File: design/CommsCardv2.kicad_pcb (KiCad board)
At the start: 4 copper layers, 191 parts, among them J1001 USB_B, J201 Conn_01x02, J301 DB9_Male_MountingHoles, J302 DB9_Male_MountingHoles, J303 DB9_Male_MountingHoles, J304 Conn_01x02, J305 Conn_Coaxial, J501 Conn_01x03, J701 Conn_01x03, J901 USB_B, Q301 Q_NMOS_DGS, Q302 Q_NMOS_DGS, U1001 ADUM3160, U201 LT3509EMSE, U301 MAX3387EEUG, U302 MAX3485, U303 TPS28225DRBT, U401 74LV14, U402 74LVC2G00, U403 STWD100xxWY, U404 STWD100xxWY, U405 74AHC157, U501 93C46B, U502 FT4232H, U503 74LV595, U601 74LVC3G14, U602 SN74LV86, U603 501BMILF, U604 74LVC1G80, U605 74LV595, U606 74LV595, U701 93C46B, U702 FT4232H, U703 74LV595, U801 74LVC3G14, U802 SN74LV86, U803 501BMILF, U804 74LVC1G80, U805 74LV595, U806 74LV595, U901 ADUM3160, X501 ASEMB-12MHz, X701 ASEMB-12MHz

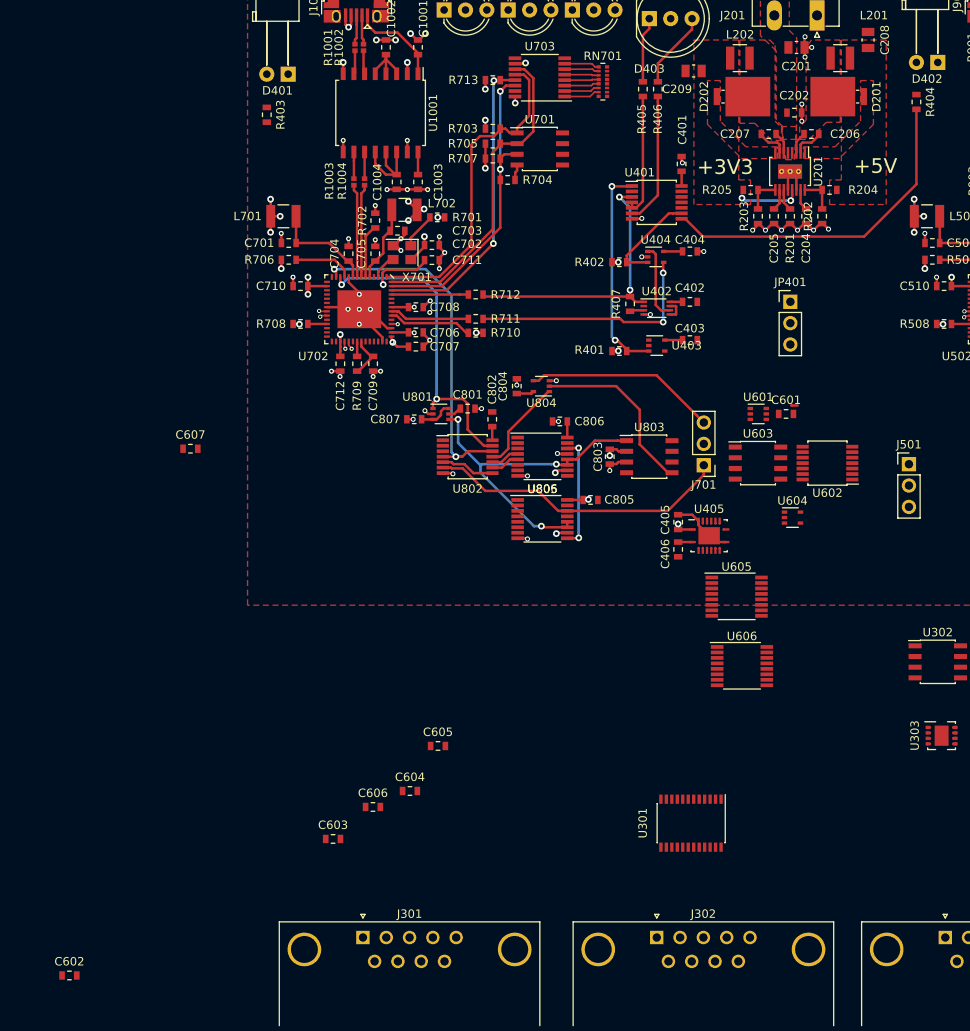
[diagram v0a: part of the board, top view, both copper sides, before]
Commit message: Further LOS updates.  Compressing space
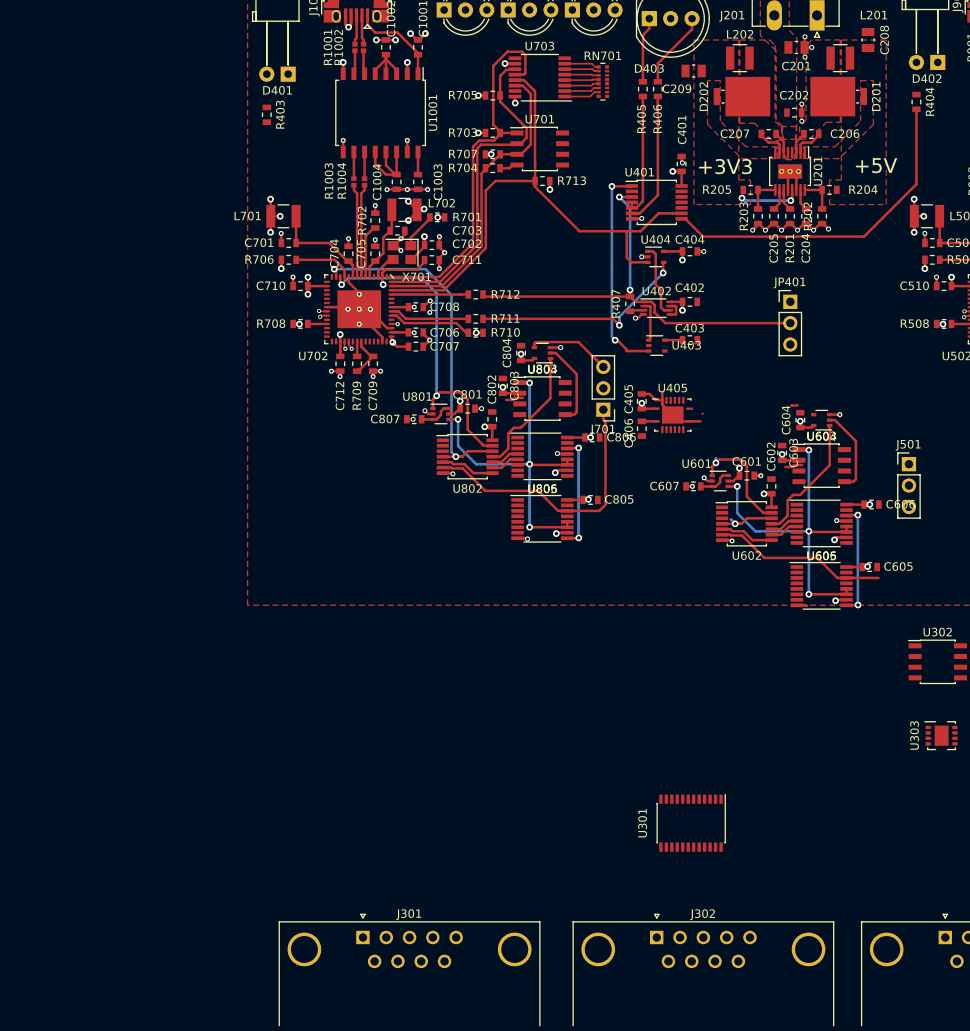
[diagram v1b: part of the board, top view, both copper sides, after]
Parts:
- removed R401, R402: 10k, Resistor_SMD:R_0603_1608Metric
- moved C602 101.7 mm to (137.5, 98.8), turned to 90 degrees
- moved C603 70.4 mm to (138.7, 94.8), turned to 90 degrees
- moved C606 69.3 mm to (149.4, 100.9)
- moved C604 64.0 mm to (140.9, 90.9), turned to 90 degrees
- moved C607 60.0 mm to (128.2, 98.8), turned to 180 degrees
- moved C605 55.6 mm to (149.1, 108.4)
- moved U606 19.4 mm to (143.4, 103.2)
- moved C803 15.2 mm to (105.5, 86.8), turned to 90 degrees
- moved C405 15.0 mm to (122.0, 88.7)
- moved C406 15.0 mm to (122.0, 91.9)
- moved U405 15.0 mm to (125.7, 90.3)
- moved U803 14.5 mm to (110.2, 88.3)
- moved J701 13.6 mm to (117.5, 89.7)
- moved R713 13.4 mm to (110.2, 62.5), turned to 0 degrees
- moved U604 12.1 mm to (143.4, 90.9), turned to 180 degrees
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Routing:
- net /FlightComputer1/LOSComms/DELAY_CLK: track 0.00 -> 42.3 mm, vias 0 -> 4
- net (no net): track 0.00 -> 23.1 mm, vias 0 -> 1
- net +3V3: track 107.9 -> 129.0 mm, vias 46 -> 60
- net /FlightComputer1/LOSComms/RNRZ-L: track 0.00 -> 20.7 mm
- net /Watchdog/~FC2_PWREN: track 48.2 -> 67.5 mm, vias 2 -> 0
- net /FlightComputer1/IN_CHARGE: track 35.0 -> 54.0 mm
- net /FlightComputer1/LOSComms/CLK: track 0.00 -> 13.8 mm, vias 0 -> 1
- net Net-(U605-Pad9): track 0.00 -> 13.5 mm, vias 0 -> 2
- net /FlightComputer2/LOSComms/BIPHASE: track 22.9 -> 9.97 mm
- net /FlightComputer2/LOSComms/2xCLOCK: track 21.3 -> 10.2 mm
- net /FlightComputer1/LOSComms/2xCLOCK: track 0.00 -> 10.2 mm
- net GND: track 119.5 -> 128.0 mm, vias 80 -> 82
- net /FlightComputer2/EECS: track 38.9 -> 45.8 mm
- net Net-(U602-Pad5): track 0.00 -> 6.44 mm
- net /Watchdog/FC1_WDO: track 0.00 -> 4.86 mm
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
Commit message: Minimizing space in design
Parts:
- D403: footprint LED_THT:LED_D8.0mm-3 -> LEDs:WP130WDT
- D501, D502, D503, D701, D702, D703: footprint LED_THT:LED_D5.0mm-3 -> LEDs:WP130WDT
- moved RN701 14.2 mm to (104.2, 45.5), turned to 90 degrees
- moved R705 14.1 mm to (101.0, 66.0), turned to 90 degrees
- moved D403 8.73 mm to (131.5, 41.5), turned to 180 degrees
- moved U703 5.83 mm to (104.2, 51.0), turned to 270 degrees
- moved D501 5.08 mm to (200.4, 41.3), turned to 180 degrees
- moved D502 5.08 mm to (192.8, 41.3), turned to 180 degrees
- moved D503 5.08 mm to (185.2, 41.3), turned to 180 degrees
- moved U701 4.70 mm to (105.7, 60.7)
- moved R707 4.40 mm to (101.0, 62.2), turned to 270 degrees
- moved R713 3.81 mm to (107.0, 64.5)
- moved R704 3.57 mm to (103.8, 64.5), turned to 0 degrees
- moved R703 3.52 mm to (101.0, 57.9), turned to 90 degrees
- moved C1001 1.07 mm to (94.6, 47.3), turned to 180 degrees
- moved D701 0.58 mm to (114.4, 42.2), turned to 180 degrees
- moved D702 0.58 mm to (106.7, 42.2), turned to 180 degrees
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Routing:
- net /Watchdog/FC2_WD: track 26.2 -> 0.00 mm, vias 2 -> 0
- net /Watchdog/~FC2_PWREN: track 67.5 -> 49.2 mm
- net /FlightComputer1/IN_CHARGE: track 54.0 -> 36.4 mm
- net Net-(R406-Pad1): track 15.7 -> 0.00 mm
- net Net-(R405-Pad1): track 14.7 -> 0.00 mm
- net /FlightComputer2/EECS: track 45.8 -> 35.3 mm
- net Net-(D403-Pad3): track 9.19 -> 0.00 mm
- net GND: track 128.0 -> 119.6 mm
- net /FlightComputer2/EECLK: track 40.6 -> 32.3 mm
- net Net-(D403-Pad1): track 7.82 -> 0.00 mm
- net /FC2_USB/USB_GND: track 10.5 -> 3.14 mm, vias 7 -> 0
- net Net-(RN701-Pad7): track 4.26 -> 0.00 mm
- net Net-(RN701-Pad1): track 4.20 -> 0.00 mm
- net Net-(RN701-Pad6): track 4.20 -> 0.00 mm
- net Net-(RN701-Pad2): track 4.14 -> 0.00 mm
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- added copper zone on F.Cu, net /FC2_USB/USB_GND
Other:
- net class Default: via_dia 0.8 -> 0.6; via_drill 0.4 -> 0.35
- net class NetConn: via_dia 0.8 -> 0.6; via_drill 0.4 -> 0.35

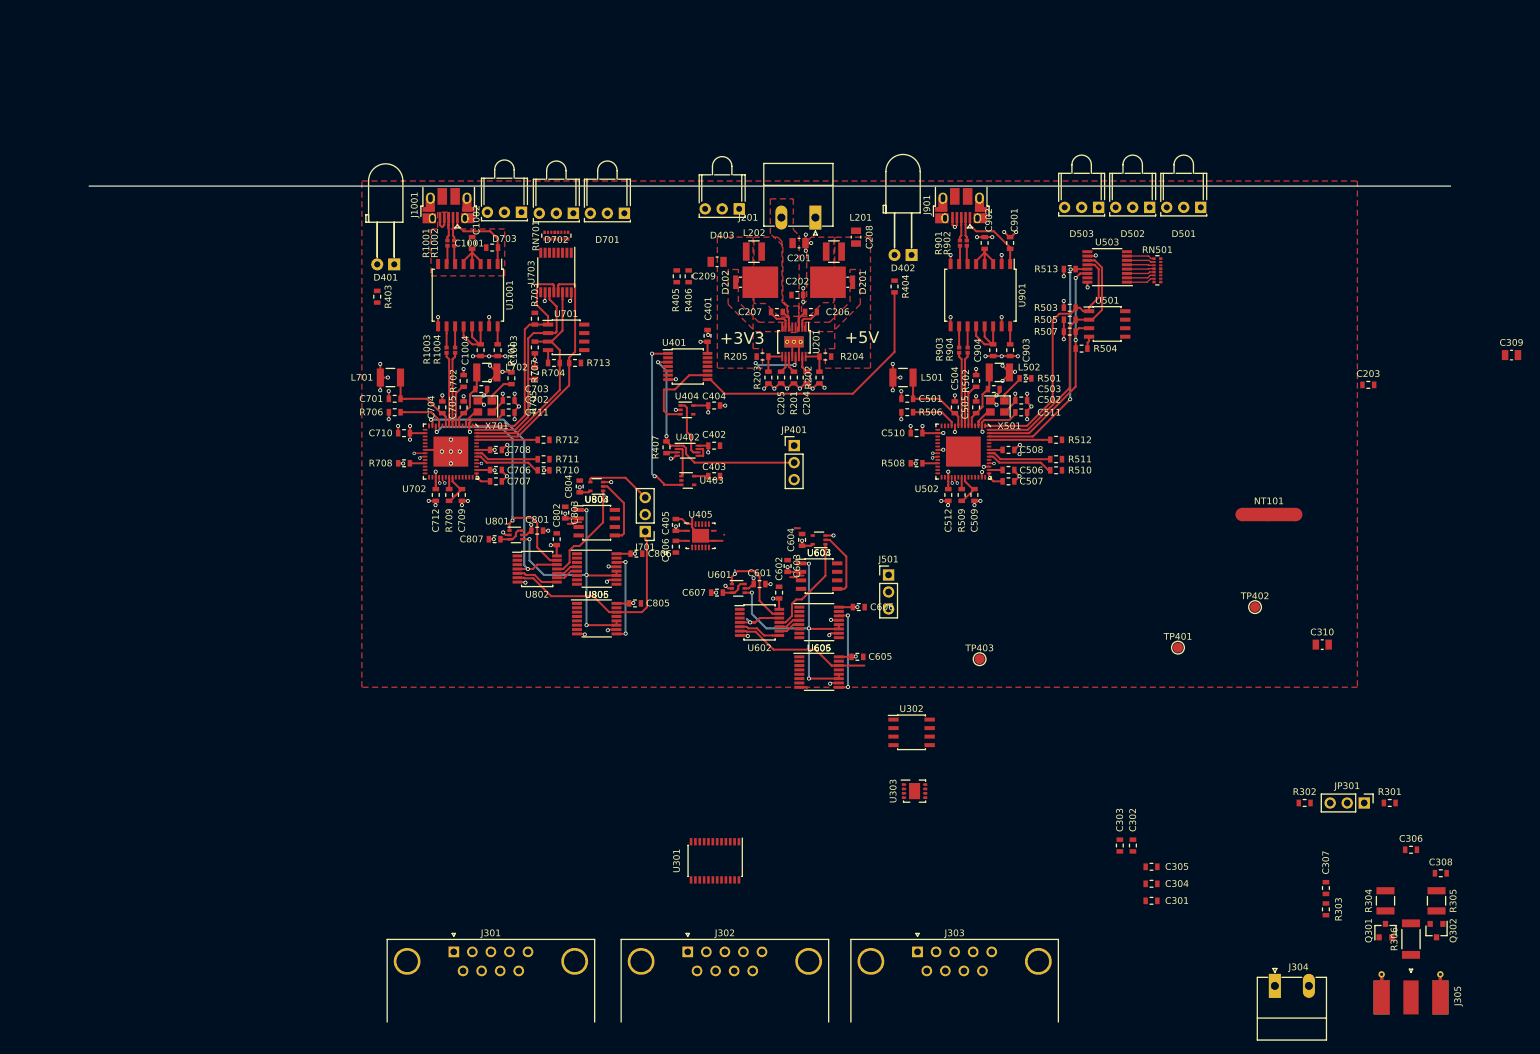
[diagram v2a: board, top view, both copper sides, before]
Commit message: Switching to light pipes for LEDs
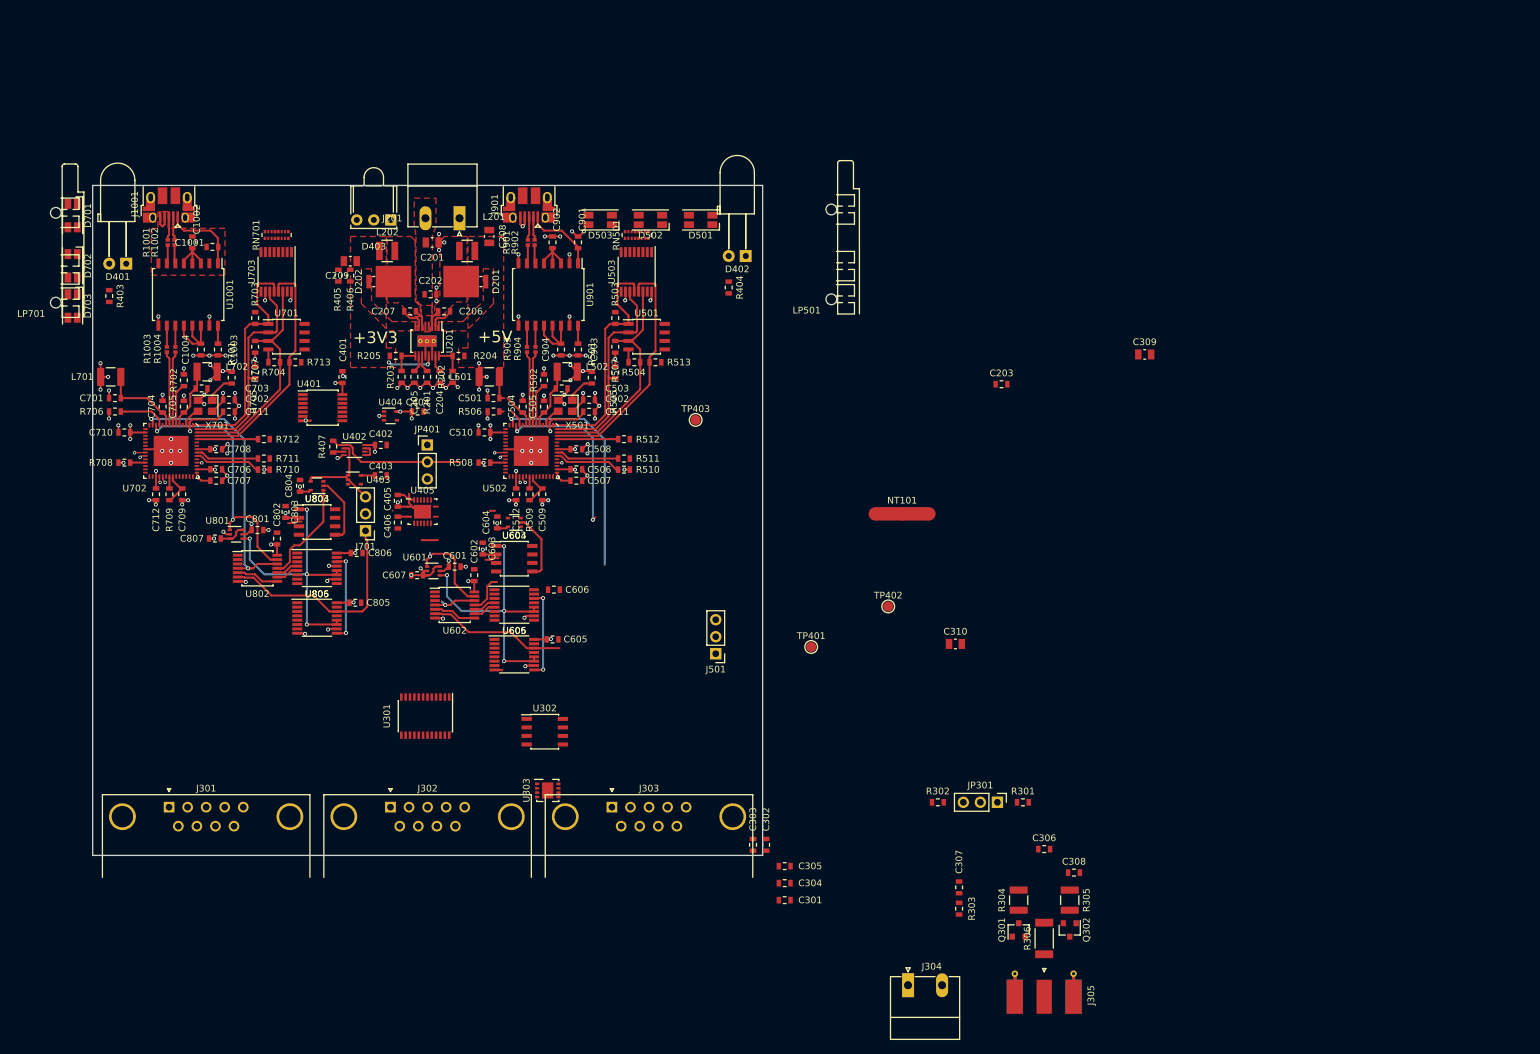
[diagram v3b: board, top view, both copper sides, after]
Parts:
- added LP501: LightPipe, LEDs:LightPipe DiaLight 515-1064, F.Cu at (145.2, 55.0)
- added LP701: LightPipe, LEDs:LightPipe DiaLight 515-1064, F.Cu at (29.5, 55.5)
- D501, D502, D503, D701, D702, D703: value WP130WDT/EGW -> LTST-C155GYKT; footprint LEDs:WP130WDT -> LED_SMD:LED_RGB_1210
- moved D701 82.4 mm to (32.0, 42.5), turned to 270 degrees
- moved RN501 77.9 mm to (116.2, 45.4), turned to 90 degrees
- moved D702 75.2 mm to (32.0, 50.0), turned to 270 degrees
- moved D501 74.7 mm to (125.8, 43.1)
- moved D502 74.5 mm to (118.2, 43.1)
- moved D503 74.4 mm to (110.8, 43.1)
- moved U503 70.3 mm to (116.2, 50.9), turned to 270 degrees
- moved U501 68.8 mm to (117.7, 60.6)
- moved D703 68.4 mm to (32.0, 56.0), turned to 270 degrees
- moved R505 68.3 mm to (113.0, 65.9), turned to 90 degrees
- moved R507 67.9 mm to (113.0, 62.1), turned to 270 degrees
- moved R503 67.9 mm to (113.0, 57.8), turned to 90 degrees
- moved R504 66.8 mm to (115.8, 64.4), turned to 0 degrees
- moved R501 64.7 mm to (109.5, 66.7), turned to 90 degrees
- moved C503 64.5 mm to (105.0, 68.3)
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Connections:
- D501 pad 2: GND -> Net-(D501-Pad2)
- D502 pad 2: GND -> Net-(D502-Pad2)
- D503 pad 2: GND -> Net-(D503-Pad2)
- D503 pad 3: Net-(D503-Pad3) -> GND
- D701 pad 2: GND -> Net-(D701-Pad2)
- D702 pad 2: GND -> Net-(D702-Pad2)
- D703 pad 2: GND -> Net-(D703-Pad2)
- D703 pad 3: Net-(D703-Pad3) -> GND
- RN501 pad 11: Net-(D501-Pad1) -> Net-(D501-Pad2)
- RN501 pad 12: Net-(D501-Pad3) -> Net-(D501-Pad1)
- RN501 pad 13: Net-(D502-Pad1) -> Net-(D502-Pad2)
- RN501 pad 14: Net-(D502-Pad3) -> Net-(D502-Pad1)
- RN501 pad 15: Net-(D503-Pad1) -> Net-(D503-Pad2)
- RN501 pad 16: Net-(D503-Pad3) -> Net-(D503-Pad1)
- RN701 pad 11: Net-(D701-Pad1) -> Net-(D701-Pad2)
- RN701 pad 12: Net-(D701-Pad3) -> Net-(D701-Pad1)
- RN701 pad 13: Net-(D702-Pad1) -> Net-(D702-Pad2)
- RN701 pad 14: Net-(D702-Pad3) -> Net-(D702-Pad1)
- RN701 pad 15: Net-(D703-Pad1) -> Net-(D703-Pad2)
- RN701 pad 16: Net-(D703-Pad3) -> Net-(D703-Pad1)
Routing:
- net Net-(R404-Pad2): track 40.3 -> 0.00 mm
- net /FlightComputer1/LOSComms/DATA: track 0.00 -> 34.9 mm, vias 0 -> 1
- net /FlightComputer1/LOSComms/CLK: track 13.8 -> 39.9 mm, vias 1 -> 3
- net /Watchdog/~FC1_PWREN: track 61.8 -> 36.0 mm, vias 4 -> 0
- net /FlightComputer1/IN_CHARGE: track 36.4 -> 22.6 mm, vias 2 -> 0
- net /Watchdog/~FC2_PWREN: track 49.2 -> 36.0 mm
- net (no net): track 23.1 -> 13.4 mm
- net /Watchdog/FC2_WDO: track 8.86 -> 0.00 mm
- net /FlightComputer1/EECLK: track 38.7 -> 32.3 mm
- net Net-(RN501-Pad7): track 4.26 -> 0.00 mm
- net Net-(RN501-Pad1): track 4.20 -> 0.00 mm
- net Net-(RN501-Pad6): track 4.20 -> 0.00 mm
- net /FlightComputer1/EEDATA: track 38.0 -> 33.9 mm, vias 2 -> 0
- net Net-(RN501-Pad2): track 4.14 -> 0.00 mm
- net Net-(RN501-Pad5): track 4.13 -> 0.00 mm
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- removed copper zone on GND1.Cu, net /FC1_USB/USB_GND
- removed copper zone on PWR2.Cu, net /FlightComputer1/1V8
- removed copper zone on F.Cu, net GND
- removed copper zone on GND1.Cu, net GND
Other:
- board outline added: 100 x 100 mm
